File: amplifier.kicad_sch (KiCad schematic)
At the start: 1 part, among them U5 PAM8403D

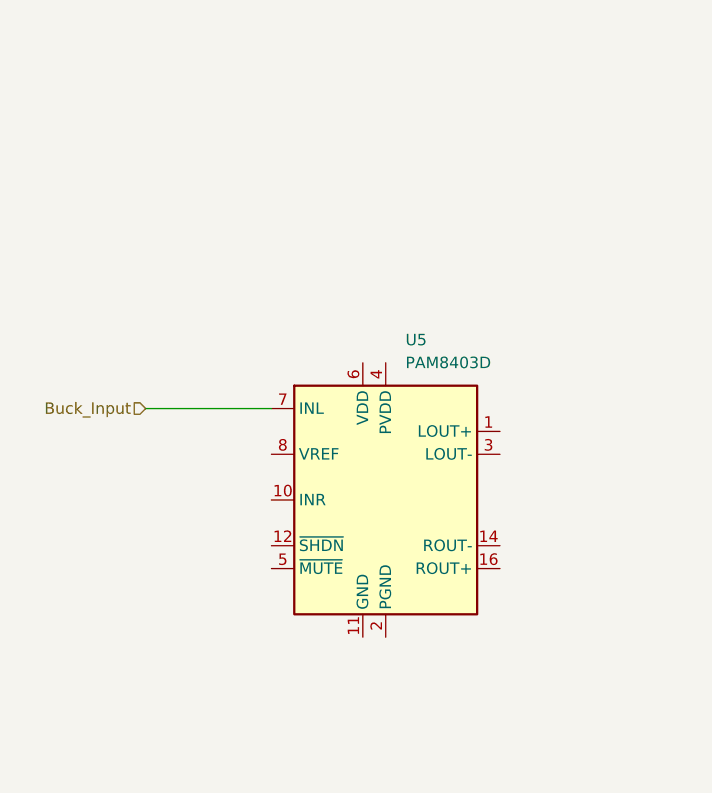
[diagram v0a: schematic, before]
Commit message: Made Audio Amplifier Connections
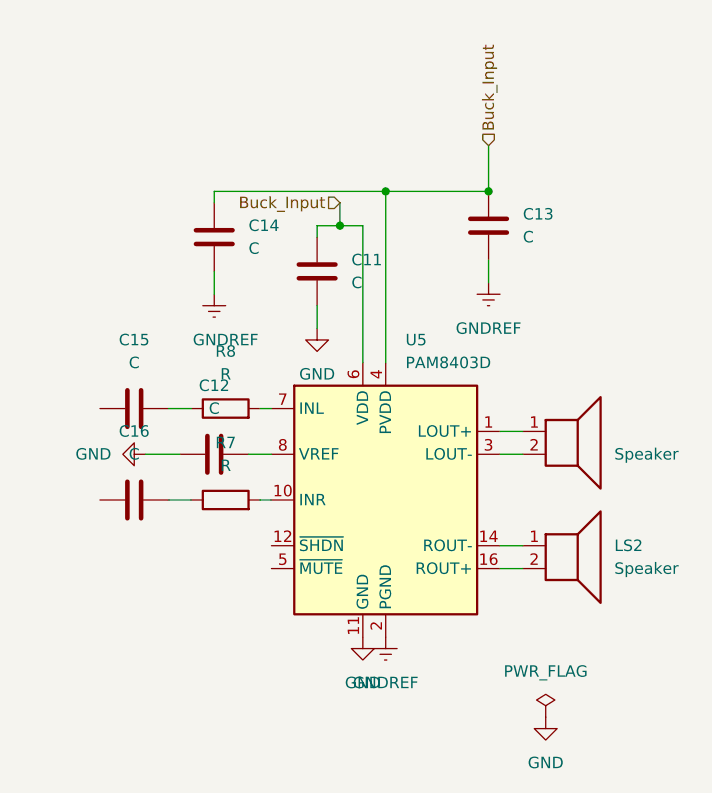
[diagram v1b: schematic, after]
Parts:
- added C11, C12, C13, C14, C15, C16: C, symbol Device:C
- added LS1, LS2: Speaker, symbol Device:Speaker
- added R7, R8: R, symbol Device:R
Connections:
- net Buck_Input: now also U5.13 (PVDD), U5.4 (PVDD), U5.6 (VDD), C11.1, C13.1, C14.1; no longer U5.7 (INL)
- net at U5.1 (LOUT+): now also LS1.1
- net at U5.10 (INR): now also R7.2
- net GND: now reaches U5.11 (GND)
- net GND: now also C11.2, C12.1
- net at U5.14 (ROUT-): now also LS2.1
- net GNDREF: now reaches U5.15 (PGND), U5.2 (PGND)
- net GNDREF: now also C13.2, C14.2
- net at U5.16 (ROUT+): now also LS2.2
- net at U5.3 (LOUT-): now also LS1.2
- net at U5.8 (VREF): now also C12.2
- new net: C16.2, R7.1
- new net: C15.2, R8.1
- new net: R8.2, U5.7 (INL)

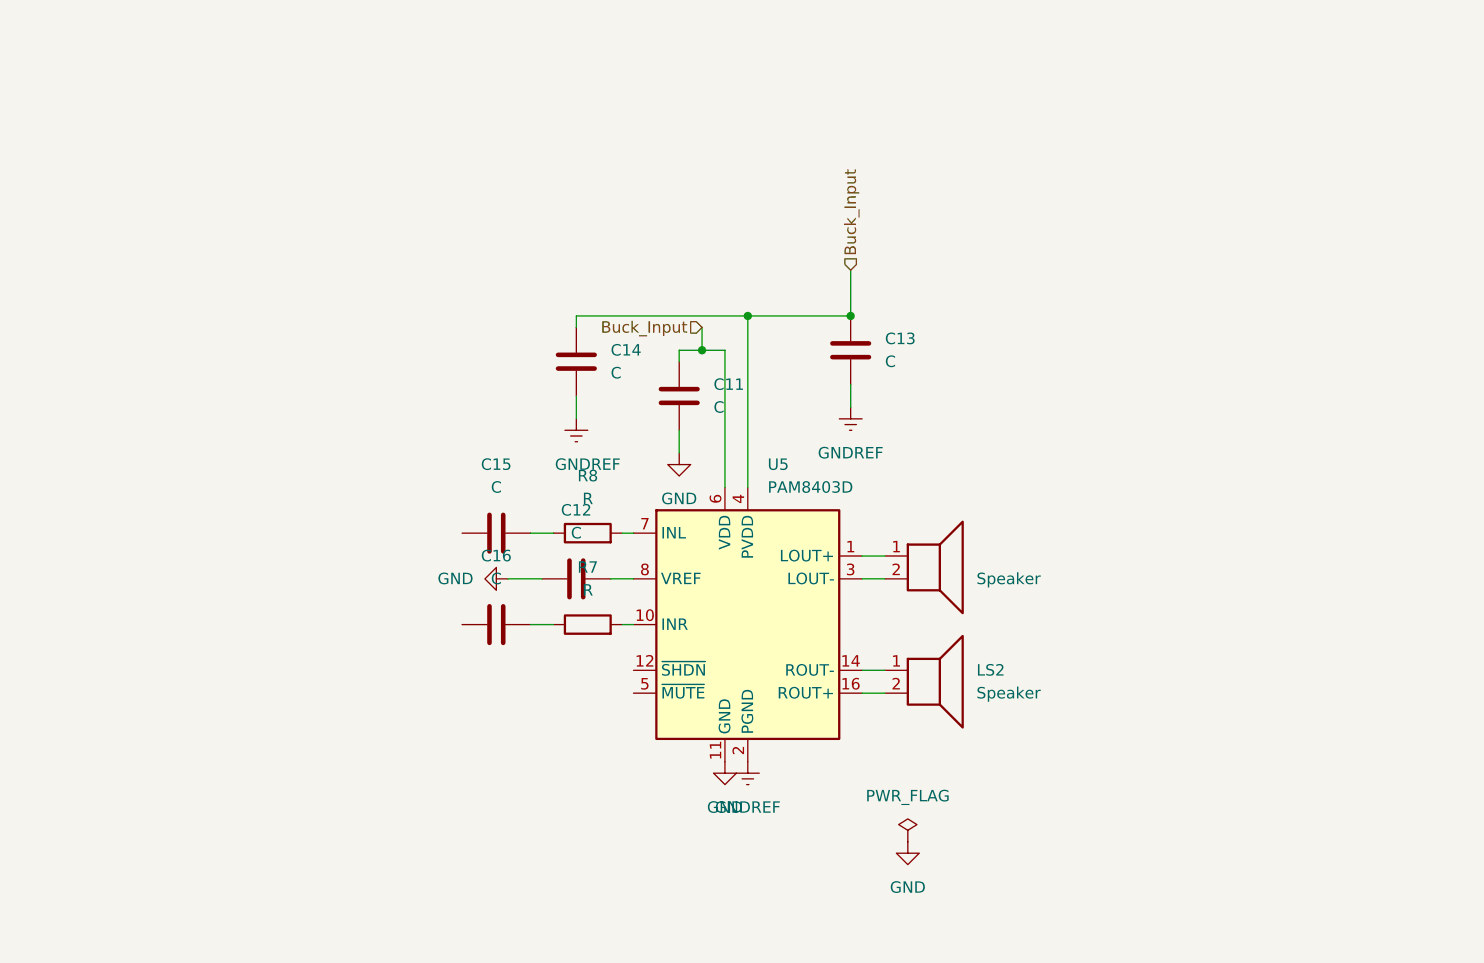
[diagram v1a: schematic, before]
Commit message: Finished AudioAmplifier + Added Values
Added Buck Coverter components values, finished audio amplifier
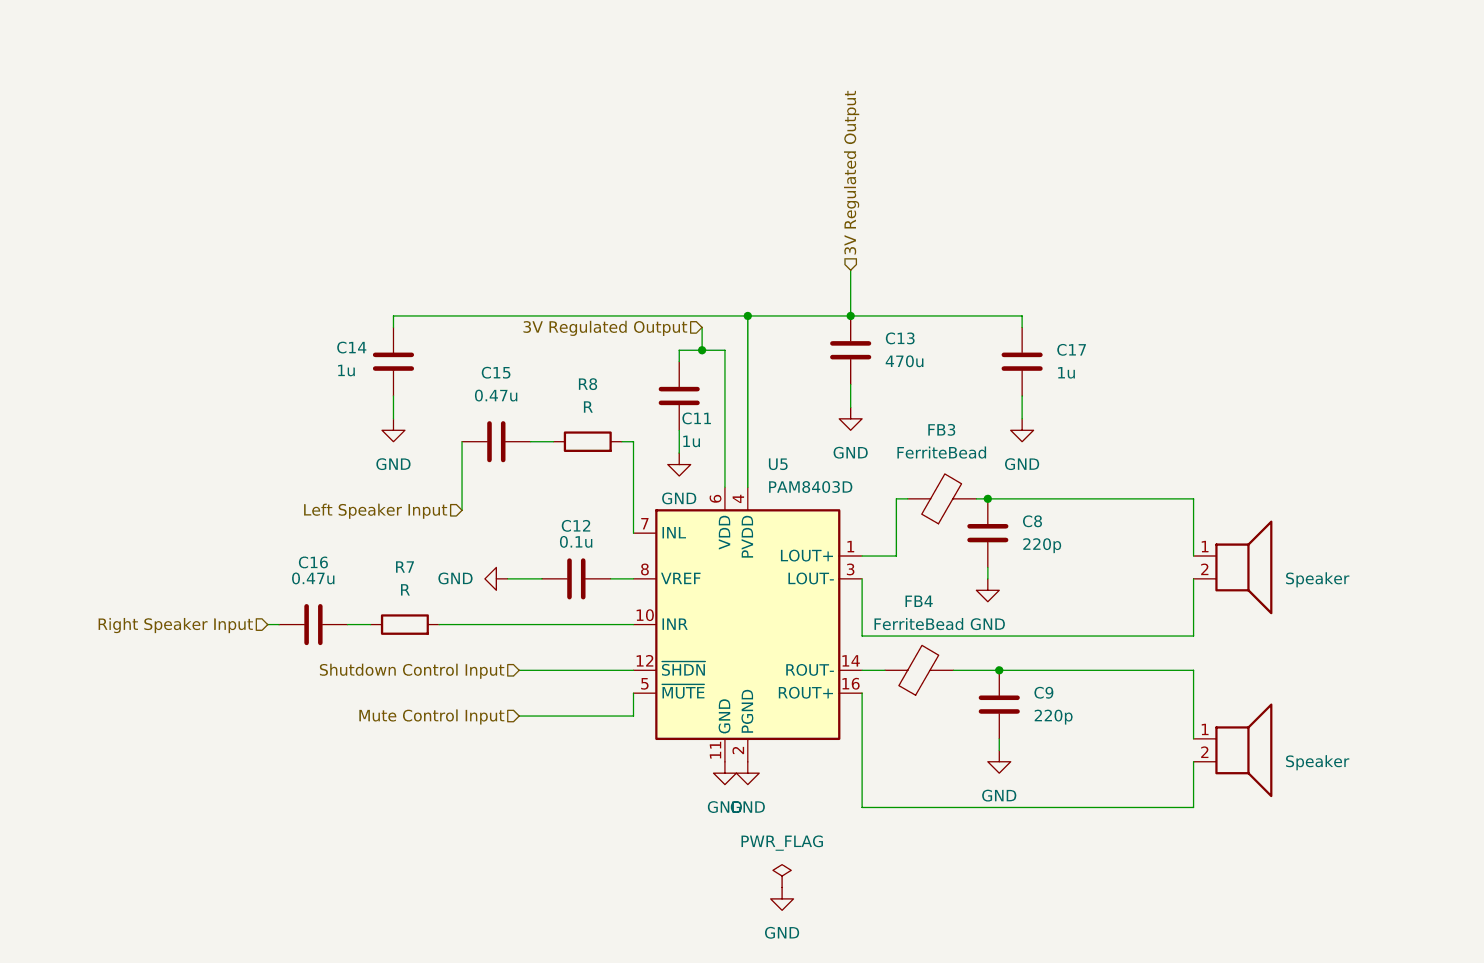
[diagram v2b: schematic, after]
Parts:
- added C17: 1u, symbol Device:C
- added C8, C9: 220p, symbol Device:C
- added FB3, FB4: FerriteBead, symbol Device:FerriteBead
- C11, C14: value C -> 1u
- C12: value C -> 0.1u
- C13: value C -> 470u
- C15, C16: value C -> 0.47u
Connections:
- net GNDREF is gone; now on net GND: C13.2, C14.2, U5.15 (PGND), U5.2 (PGND)
- net GND: now also C17.2, C8.2, C9.2
- net Right Speaker Input: now reaches C16.1
- net Left Speaker Input: now reaches C15.1
- net at U5.1 (LOUT+): now also FB3.1; no longer LS1.1
- net Shutdown Control Input: now reaches U5.12 (~{SHDN})
- net at U5.14 (ROUT-): now also FB4.1; no longer LS2.1
- net Mute Control Input: now reaches U5.5 (~{MUTE})
- net Buck_Input renamed 3V Regulated Output
- net 3V Regulated Output: now also C17.1
- new net: C8.1, FB3.2, LS1.1
- new net: C9.1, FB4.2, LS2.1
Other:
- moved on the sheet: C14, C15, C16, R7, R8

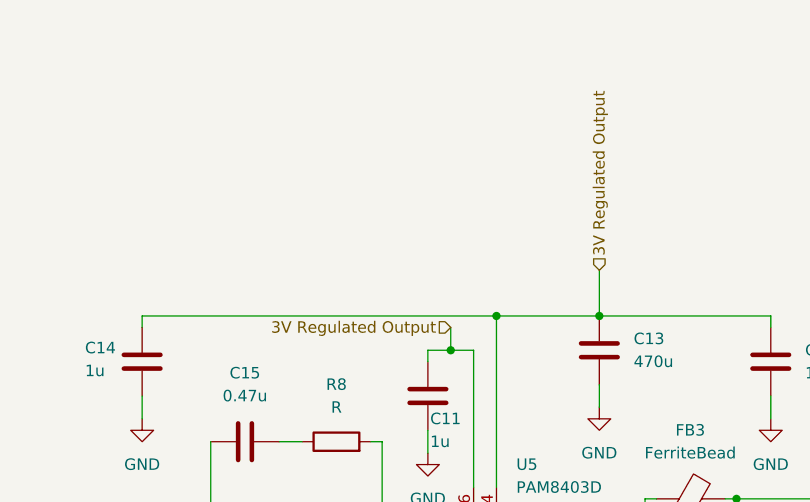
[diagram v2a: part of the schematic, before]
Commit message: Set 3.3 Output from Buck
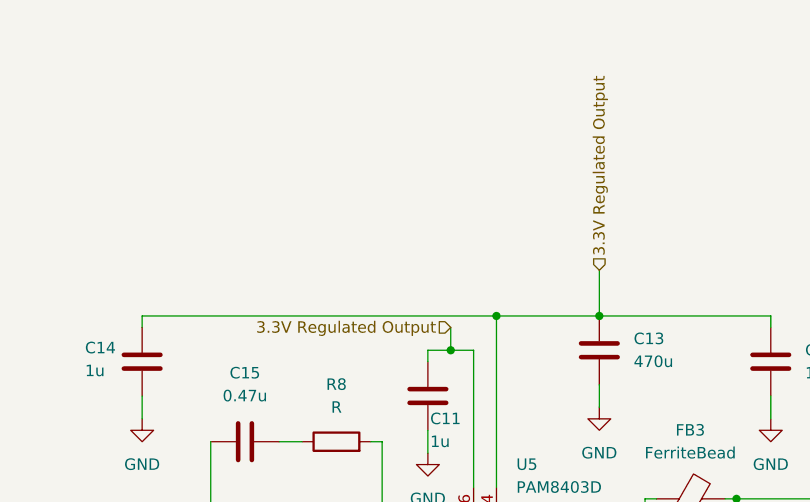
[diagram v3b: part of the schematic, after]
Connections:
- net 3V Regulated Output renamed 3.3V Regulated Output
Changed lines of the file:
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@@
 		)
 	)
-	(hierarchical_label "3V Regulated Output"
+	(hierarchical_label "3.3V Regulated Output"
 		(shape input)
 		(at 146.05 53.34 90)
@@
 		)
 	)
-	(hierarchical_label "3V Regulated Output"
+	(hierarchical_label "3.3V Regulated Output"
 		(shape input)
 		(at 129.54 59.69 180)

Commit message: Cleanup, sorting, adding external parts
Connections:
- net 3.3V Regulated Output renamed 3.3V_IN
- net Left Speaker Input renamed L_IN
- net Mute Control Input renamed MUTE_IN
- net Right Speaker Input renamed R_IN
- net Shutdown Control Input renamed SHDN_IN
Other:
- note added: "Left Speaker Input"
- note added: "Mute Control Signal"
- note added: "Right Speaker Input"
- note added: "Shutdown Control Signal"
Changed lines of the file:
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@@
 		)
 	)
-	(hierarchical_label "Mute Control Input"
+	(text "Left Speaker Input"
+		(exclude_from_sim no)
+		(at 87.122 80.264 0)
+		(effects
+			(font
+				(size 1.27 1.27)
+			)
+		)
+	)
+	(text "Mute Control Signal"
+		(exclude_from_sim no)
+		(at 89.154 103.124 0)
+		(effects
+			(font
+				(size 1.27 1.27)
+			)
+		)
+	)
+	(text "Right Speaker Input"
+		(exclude_from_sim no)
+		(at 65.278 92.964 0)
+		(effects
+			(font
+				(size 1.27 1.27)
+			)
+		)
+	)
+	(text "Shutdown Control Signal"
+		(exclude_from_sim no)
+		(at 87.122 98.044 0)
+		(effects
+			(font
+				(size 1.27 1.27)
+			)
+		)
+	)
+	(hierarchical_label "MUTE_IN"
 		(shape input)
 		(at 109.22 102.87 180)
@@
 		)
 	)
-	(hierarchical_label "3.3V Regulated Output"
+	(hierarchical_label "3.3V_IN"
 		(shape input)
 		(at 146.05 53.34 90)
@@
 		)
 	)
-	(hierarchical_label "Shutdown Control Input"
+	(hierarchical_label "SHDN_IN"
 		(shape input)
 		(at 109.22 97.79 180)
@@
 		)
 	)
-	(hierarchical_label "Right Speaker Input"
+	(hierarchical_label "R_IN"
 		(shape input)
 		(at 81.28 92.71 180)
@@
 		)
 	)
-	(hierarchical_label "Left Speaker Input"
+	(hierarchical_label "L_IN"
 		(shape input)
 		(at 102.87 80.01 180)
@@
 		)
 	)
-	(hierarchical_label "3.3V Regulated Output"
+	(hierarchical_label "3.3V_IN"
 		(shape input)
 		(at 129.54 59.69 180)

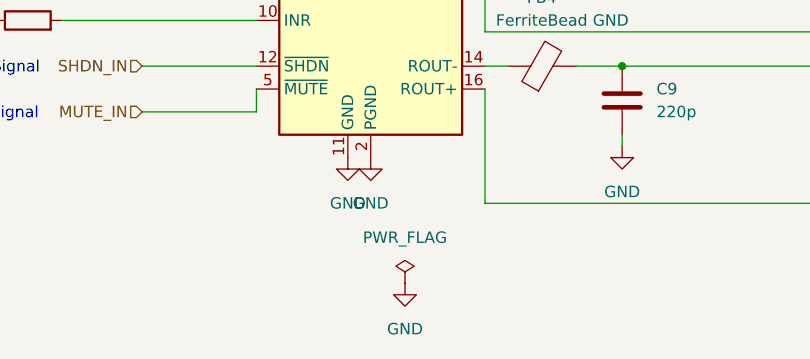
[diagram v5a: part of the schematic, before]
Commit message: Added Kitronik and cleaned connections
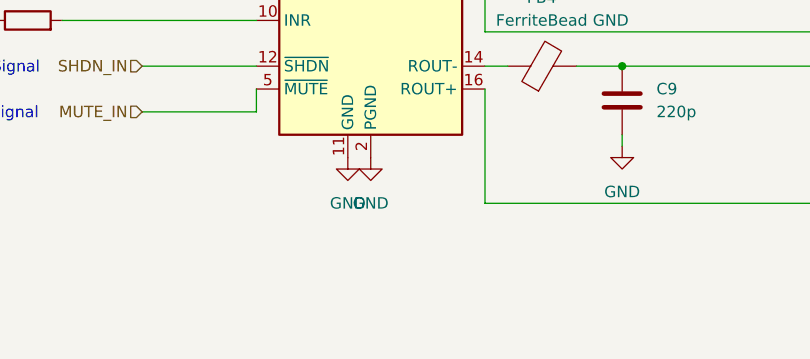
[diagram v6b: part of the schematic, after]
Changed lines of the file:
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@@
-	)
-	(symbol
-		(lib_id "power:PWR_FLAG")
-		(at 138.43 121.92 0)
-		(unit 1)
-		(exclude_from_sim no)
-		(in_bom yes)
-		(on_board yes)
-		(dnp no)
-		(fields_autoplaced yes)
-		(property "Reference" "#FLG04"
-			(at 138.43 120.015 0)
-			(effects
-				(font
-					(size 1.27 1.27)
-				)
-				(hide yes)
-			)
-		)
-		(property "Value" "PWR_FLAG"
-			(at 138.43 116.84 0)
-			(effects
-				(font
-					(size 1.27 1.27)
-				)
-			)
-		)
-		(property "Footprint" ""
-			(at 138.43 121.92 0)
-			(effects
-				(font
-					(size 1.27 1.27)
-				)
-				(hide yes)
-			)
-		)
-		(property "Datasheet" "~"
-			(at 138.43 121.92 0)
-			(effects
-				(font
-					(size 1.27 1.27)
-				)
-				(hide yes)
-			)
-		)
-		(property "Description" "Special symbol for telling ERC where power comes from"
-			(at 138.43 121.92 0)
-			(effects
-				(font
-					(size 1.27 1.27)
-				)
-				(hide yes)
-			)
-		)
-		(pin "1"
-		)
-		(instances
-			(project "plant caretaker"
-				(path "/23b35dcc-615e-4aec-abee-c26cc3d8b906/64bd70cc-1431-45fc-8946-041e9631b1bb"
-					(reference "#FLG04")
-					(unit 1)
-				)
-			)
-		)
 	)
 	(symbol
@@
 					(unit 1)
 				)
-			)
-		)
-	)
-	(symbol
-		(lib_id "power:GND")
-		(at 138.43 121.92 0)
-		(unit 1)
-		(exclude_from_sim no)
-		(in_bom yes)
-		(on_board yes)
-		(dnp no)
-		(fields_autoplaced yes)
-		(property "Reference" "#PWR010"
-			(at 138.43 128.27 0)
-			(effects
-				(font
-					(size 1.27 1.27)
-				)
-				(hide yes)
-			)
-		)
-		(property "Value" "GND"
-			(at 138.43 127 0)
-			(effects
-				(font
-					(size 1.27 1.27)
-				)
-			)
-		)
-		(property "Footprint" ""
-			(at 138.43 121.92 0)
-			(effects
-				(font
-					(size 1.27 1.27)
-				)
-				(hide yes)
-			)
-		)
-		(property "Datasheet" ""
-			(at 138.43 121.92 0)
-			(effects
-				(font
-					(size 1.27 1.27)
-				)
-				(hide yes)
-			)
-		)
-		(property "Description" "Power symbol creates a global label with name \"GND\" , ground"
-			(at 138.43 121.92 0)
-			(effects
-				(font
-					(size 1.27 1.27)
-				)
-				(hide yes)
-			)
-		)
-		(pin "1"
-		)
-		(instances
-			(project "plant caretaker"
-				(path "/23b35dcc-615e-4aec-abee-c26cc3d8b906/64bd70cc-1431-45fc-8946-041e9631b1bb"
-					(reference "#PWR010")
-					(unit 1)
-				)

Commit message: Added basic footprint to ESP32
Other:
- title: (none) -> Audio amplifier
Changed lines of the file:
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@@
 	(generator_version "8.0")
 	(paper "A4")
+	(title_block
+		(title "Audio amplifier")
+		(date "2024-12-12")
+	)
 	(junction
 		(at 129.54 62.23)

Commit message: Added more notes
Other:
- note added: "For this component, maybe make parallel connections of SMD capacitors for equivalent C? Or use electrolytic capacitor and change symbol?"
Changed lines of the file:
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@@
+		)
+	)
+	(polyline
+		(pts
+			(xy 148.59 49.53) (xy 148.59 59.69)
+		)
+		(stroke
+			(width 0)
+			(type default)
 		)
 	)
@@
 		(pts
 			(xy 162.56 105.41) (xy 162.56 106.68)
+		)
+		(stroke
+			(width 0)
+			(type default)
+		)
+	)
+	(polyline
+		(pts
+			(xy 156.21 49.53) (xy 148.59 49.53)
 		)
 		(stroke
@@
 		)
 	)
+	(text "For this component, maybe make parallel connections\nof SMD capacitors for equivalent C? \nOr use electrolytic capacitor and change symbol?"
+		(exclude_from_sim no)
+		(at 151.384 45.212 0)
+		(effects
+			(font
+				(size 1.27 1.27)
+			)
+			(justify left)
+		)
+	)
